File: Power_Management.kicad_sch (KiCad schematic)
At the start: 17 parts, among them J8 PWR_SRC_JMP, Q2 MOSFET_SI2333DDS-T1-BE3, U3 SN74LVC1G07DBVR

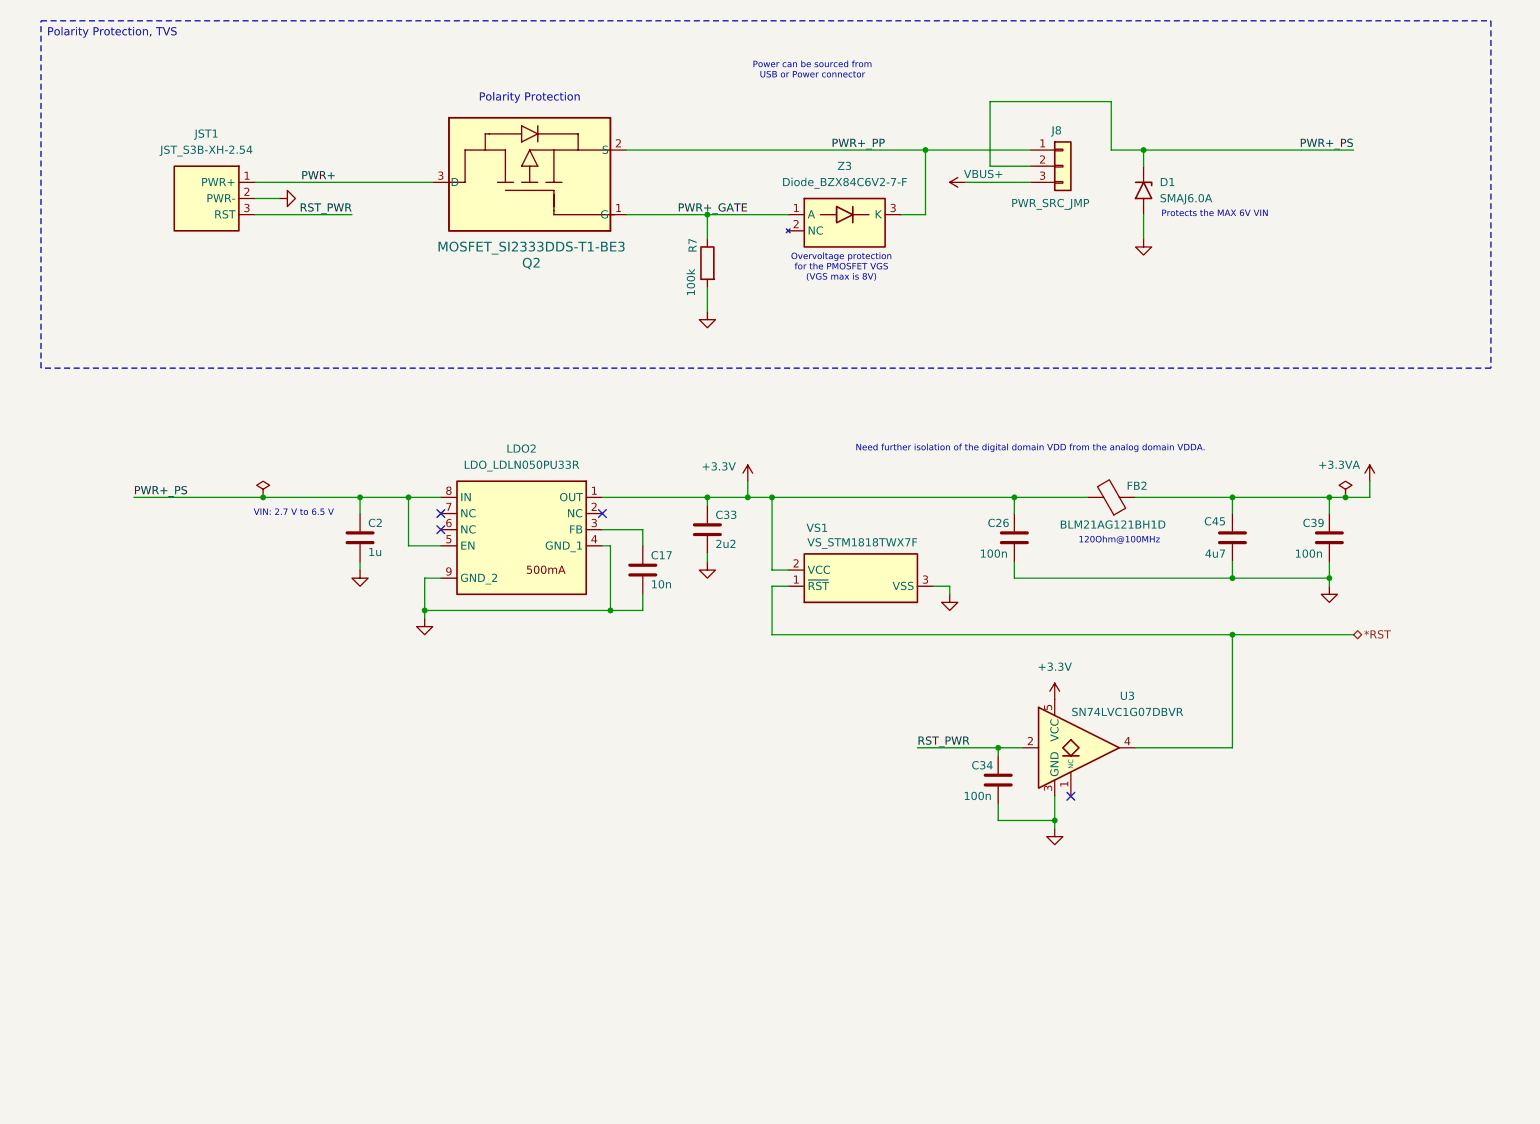
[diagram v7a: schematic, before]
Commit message: Schematics Update
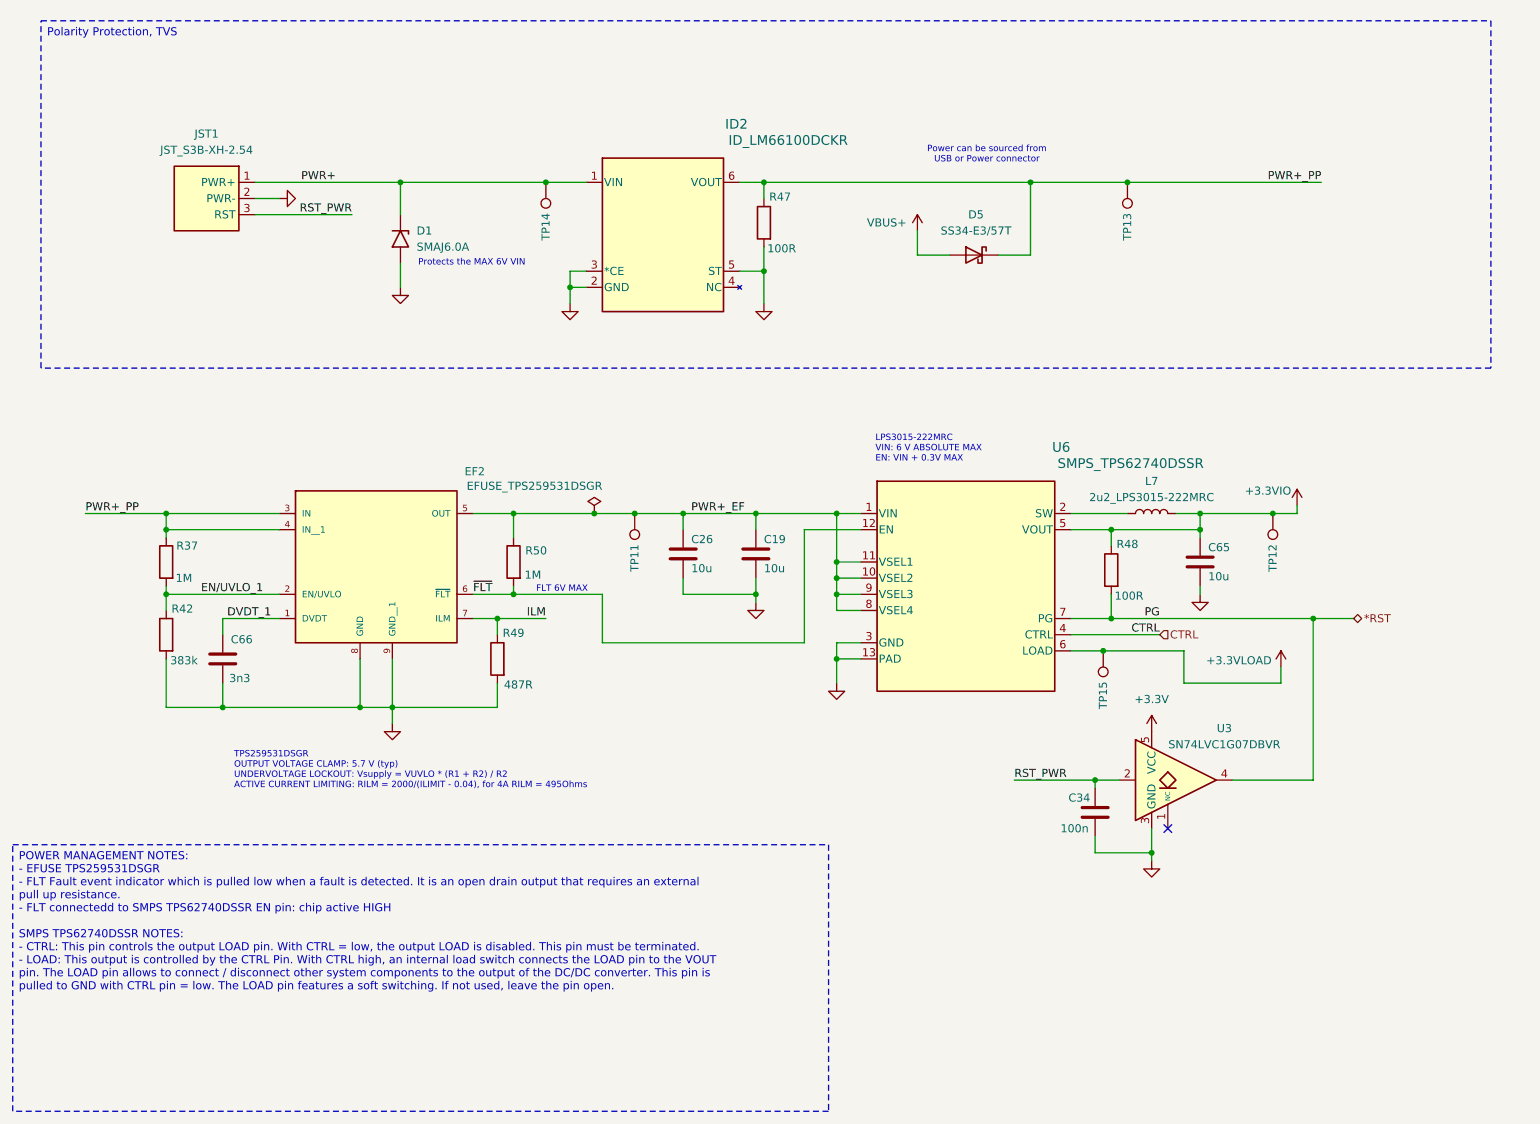
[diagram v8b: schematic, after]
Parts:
- removed C17: 10n, Capacitor_SMD:C_0805_2012Metric, symbol Device:C
- removed C2: 1u, Capacitor_SMD:C_0805_2012Metric, symbol Device:C
- removed C33: 2u2, Capacitor_SMD:C_0805_2012Metric, symbol Device:C
- removed C39: 100n, Capacitor_SMD:C_0805_2012Metric, symbol Device:C
- removed C45: 4u7, Capacitor_SMD:C_0805_2012Metric, symbol Device:C
- removed FB2: BLM21AG121BH1D, Capacitor_SMD:C_0805_2012Metric, symbol Device:FerriteBead
- removed J8: PWR_SRC_JMP, Connector_PinHeader_2.54mm:PinHeader_1x03_P2.54mm_Vertical, symbol Connector_Generic:Conn_01x03
- removed LDO2: LDO_LDLN050PU33R, Package_DFN_QFN:DFN-8-1EP_3x3mm_P0.65mm_EP1.7x2.05mm, symbol Personal_Projects:LDO_LDLN050PUR
- removed Q2: MOSFET_SI2333DDS-T1-BE3, Personal_Project:MOSFET_ SI2333DDS_SOT_DS-T1-BE3_VIS, symbol Personal_Projects:MOSFET_SI2333DDS-T1-BE3
- removed R7: 100k, Resistor_SMD:R_0805_2012Metric, symbol Device:R
- removed VS1: VS_STM1818TWX7F, Personal_Project:SOT-23-3_SOT103P237X112-3N, symbol Personal_Projects:VS_STM1813LWX7F
- removed Z3: Diode_BZX84C6V2-7-F, Personal_Project:Diode_BZX84C6V2_SOT96P240X110-3N, symbol Personal_Projects:Diode_BZX84C6V2-7-F
- added C19, C65: 10u, Capacitor_SMD:C_0805_2012Metric, symbol Device:C
- added C66: 3n3, Capacitor_SMD:C_0603_1608Metric, symbol Device:C
- added D5: SS34-E3/57T, Diode_SMD:D_SMA, symbol Diode:SS34
- added EF2: EFUSE_TPS259531DSGR, Personal_Project:EFUSE_TPS259531DSGR, symbol Personal_Projects:EFUSE_TPS259531DSGR
- added ID2: ID_LM66100DCKR, Personal_Projects:ID_LM66100DCKR, symbol Personal_Components:ID_LM66100DCKR
- added L7: 2u2_LPS3015-222MRC, Inductor_SMD:L_Coilcraft_LPS3010, symbol Device:L
- added R37, R50: 1M, Resistor_SMD:R_0603_1608Metric, symbol Device:R
- added R42: 383k, Resistor_SMD:R_0603_1608Metric, symbol Device:R
- added R47, R48: 100R, Resistor_SMD:R_0603_1608Metric, symbol Device:R
- added R49: 487R, Resistor_SMD:R_0603_1608Metric, symbol Device:R
- added TP11, TP12, TP13, TP14, TP15: TestPoint, TestPoint:TestPoint_Pad_1.5x1.5mm, symbol Connector:TestPoint
- added U6: SMPS_TPS62740DSSR, Personal_Projects:SMPS_TPS62740DSSR, symbol Personal_Components:SMPS_TPS62740DSSR
- C26: value 100n -> 10u
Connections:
- net PWR+_PS is gone; now on net PWR+: D1.1 (K)
- net *RST: now also R48.2, U6.7 (PG)
- net +3.3V: no longer C26.1
- net GND: now also C19.2, C65.2, C66.1, EF2.8 (GND), EF2.9 (GND__1), ID2.2 (GND), ID2.3 (*CE), ID2.5 (ST), R42.2, R47.2, R49.2, U6.13 (PAD), U6.3 (GND)
- net PWR+: now also ID2.1 (VIN), TP14.1
- net PWR+_PP: now also D5.1 (K), EF2.3 (IN), EF2.4 (IN__1), ID2.6 (VOUT), R37.1, R47.1, TP13.1
- net VBUS+: now also D5.2 (A)
- new net: L7.1, U6.2 (SW)
- new net +3.3VIO: C65.1, L7.2, R48.1, TP12.1, U6.5 (VOUT)
- new net +3.3VLOAD: TP15.1, U6.6 (LOAD)
- new net CTRL: U6.4 (CTRL)
- new net DVDT_1: C66.2, EF2.1 (DVDT)
- new net EN/UVLO_1: EF2.2 (EN/UVLO), R37.2, R42.1
- new net ILM: EF2.7 (ILM), R49.1
- new net PWR+_EF: C19.1, C26.1, EF2.5 (OUT), R50.1, TP11.1, U6.1 (VIN), U6.10 (VSEL2), U6.11 (VSEL1), U6.8 (VSEL4), U6.9 (VSEL3)
- new net ~{FLT}: EF2.6 (~{FLT}), R50.2, U6.12 (EN)
- no-connect marks 4 -> 1
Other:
- note added: "FLT 6V MAX"
- note added: "LPS3015-222MRC VIN: 6 V ABSOLUTE MAX EN: VIN + 0.3V MAX"
- note added: "TPS259531DSGR OUTPUT VOLTAGE CLAMP: 5.7 V (typ) UNDERVOLTAGE LOCKOUT: Vsupply = VUVLO * (R1 + R2) / R2 ACTIVE CURRENT LIMITING: RILM = 2000/(ILIMIT - 0.04), for 4A RILM = 495Ohms"
- note removed: "120Ohm@100MHz"
- note removed: "Need further isolation of the digital domain VDD from the analog domain VDDA."
- note removed: "Overvoltage protection for the PMOSFET VGS (VGS max is 8V)"
- note removed: "Polarity Protection"
- note removed: "VIN: 2.7 V to 6.5 V"
- title: LoRa Board -> LoRa STM32WL55CCU6 Board
- moved on the sheet: C34, D1, U3
